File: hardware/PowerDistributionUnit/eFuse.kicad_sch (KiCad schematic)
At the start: 45 parts, among them Q1 CSD18511Q5A, Q2 2N7002, U12 AD5258, U13 TPS25983

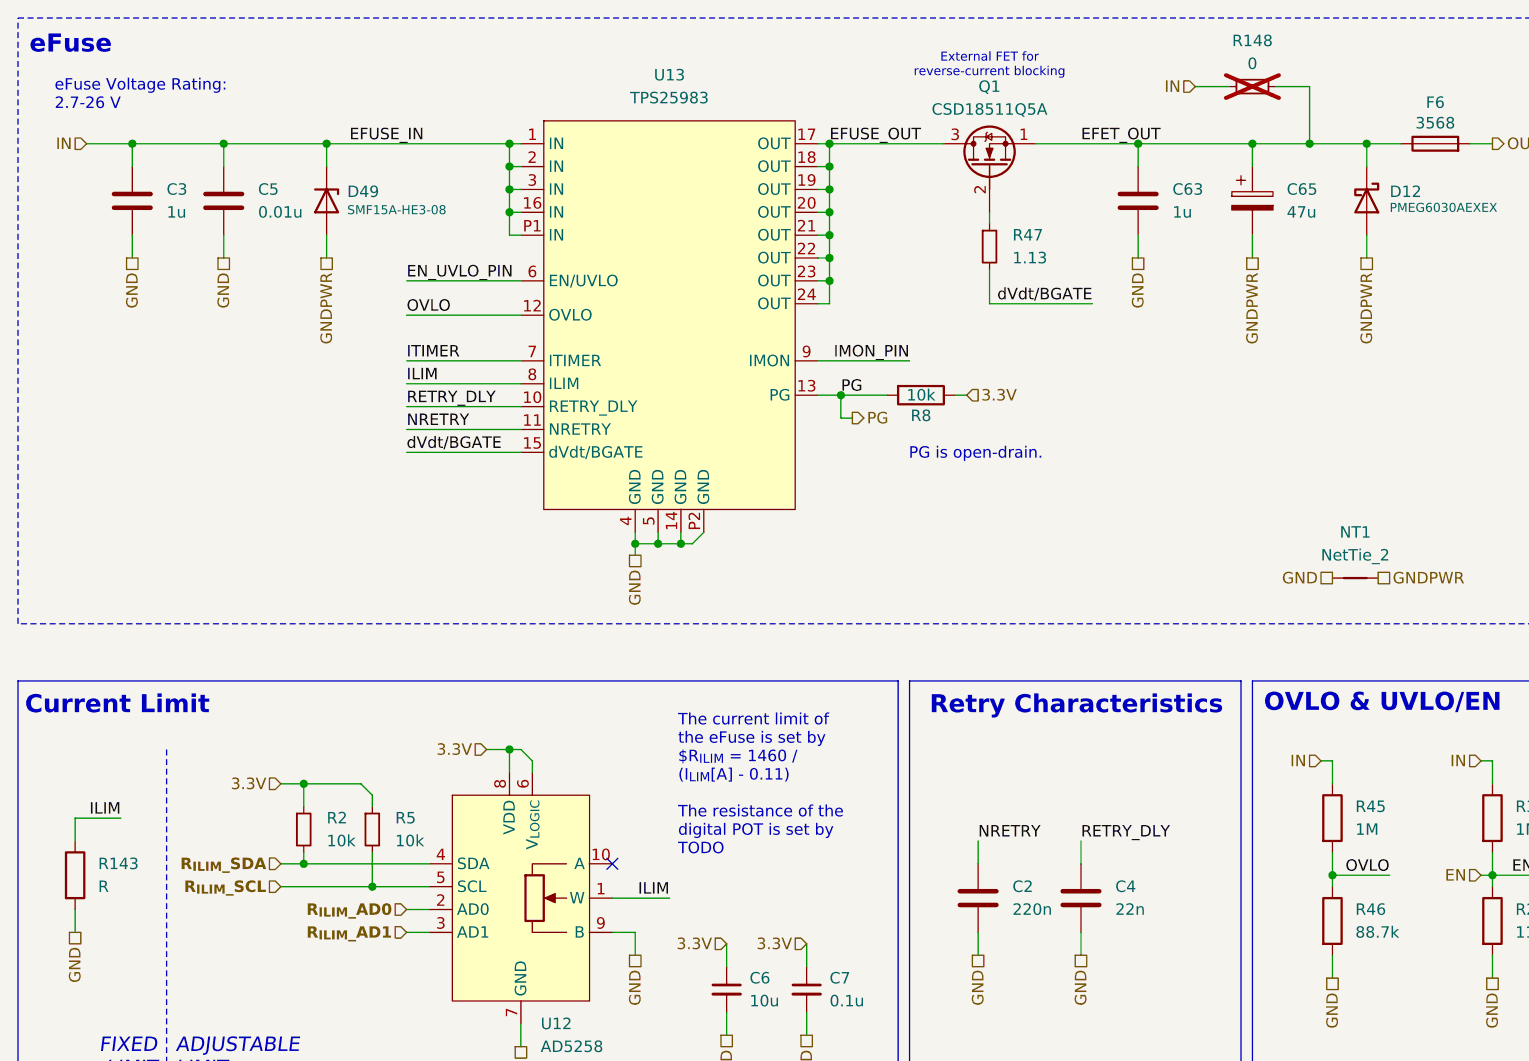
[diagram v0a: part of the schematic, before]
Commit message: started layout for general and eFuses, corrected schematic (test point footprints, bus label names, connection points, etc.), corrected footprint courtyard (eFuse, diode)
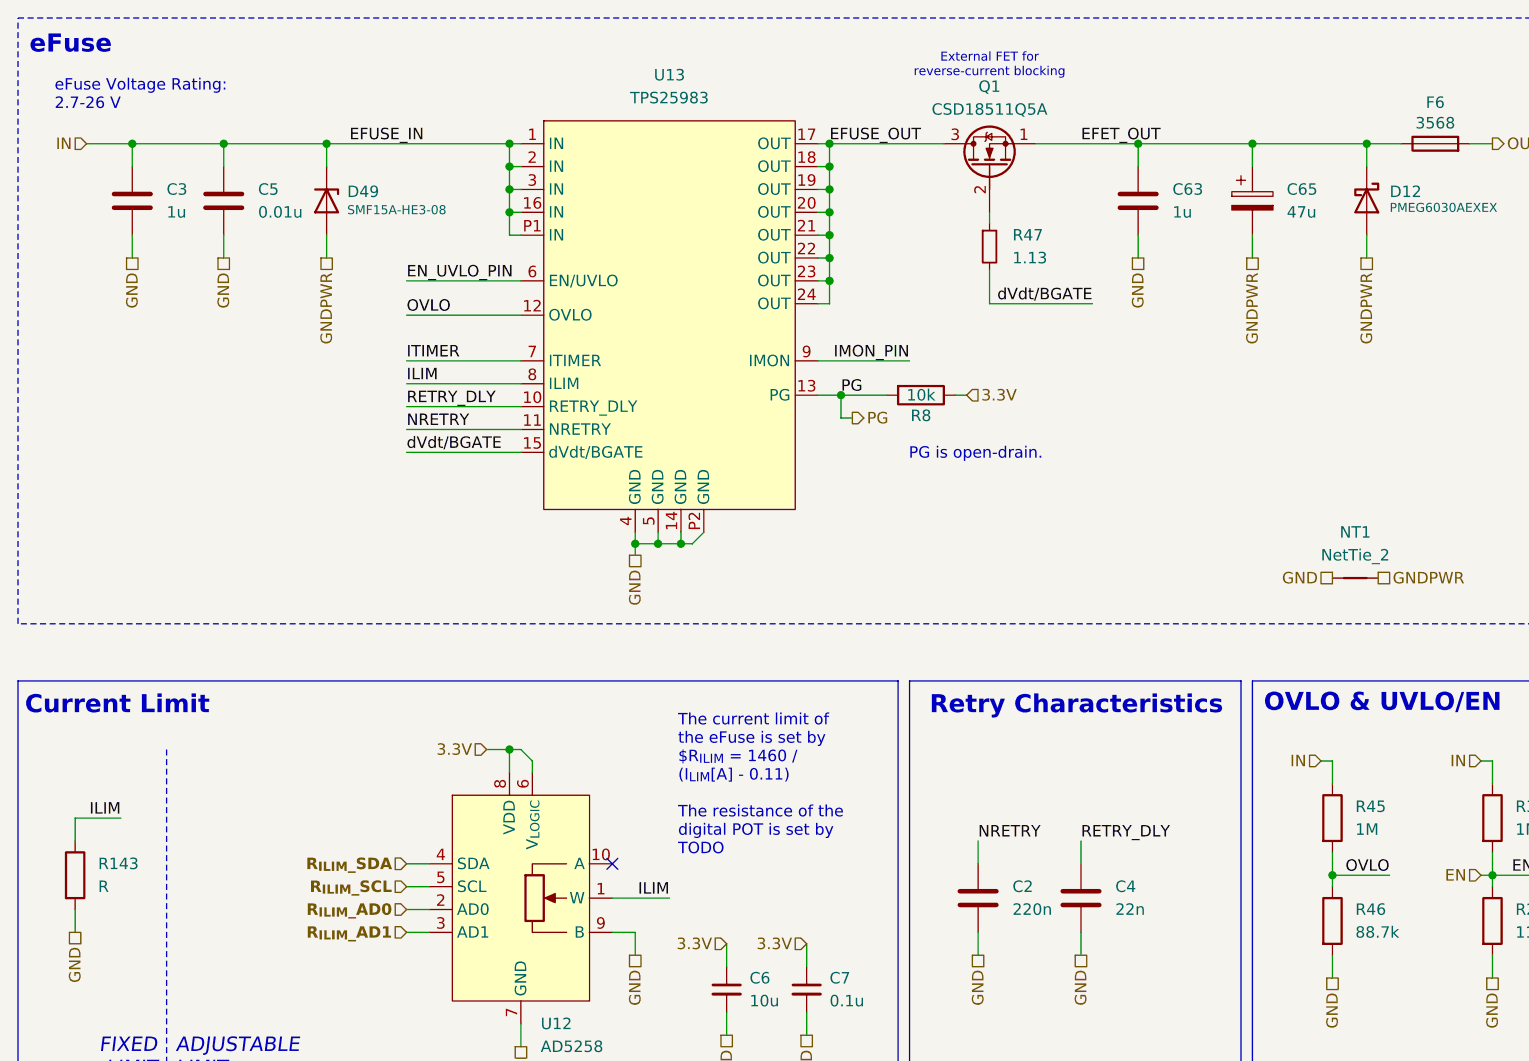
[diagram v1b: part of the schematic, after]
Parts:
- removed R148: 0, Resistor_SMD:R_0603_1608Metric, symbol Device:R_Small
- removed R2, R5: 10k, Resistor_SMD:R_0603_1608Metric, symbol Device:R_Small
- TP238: footprint Connector_PinHeader_2.54mm:PinHeader_1x01_P2.54mm_Vertical -> TestPoint:TestPoint_Pad_D1.0mm

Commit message: redid multichannel
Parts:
- added R1, R152, R263, R65: 0, Resistor_SMD:R_0603_1608Metric, symbol Device:R_Small
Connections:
- net 3.3V: now also R1.1, R65.1
- net GND: now also R152.2, R263.2
- net R_{ILIM}_AD0: no longer names the net of U12.2 (AD0)
- net R_{ILIM}_AD0: now also R1.2, R263.1
- net R_{ILIM}_AD1: no longer names the net of U12.3 (AD1)
- net R_{ILIM}_AD1: now also R152.1, R65.2
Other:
- note added: "Address Selection"
- moved on the sheet: U12
